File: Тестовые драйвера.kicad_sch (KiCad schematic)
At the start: 172 parts, among them J1 Conn_01x01, J2 Conn_01x01, J3 Conn_01x01, J4 Conn_01x01, J5 Conn_01x01, J6 Conn_02x10_Odd_Even, J7 Conn_02x10_Odd_Even, Q1 C2M0280120D, Q2 C2M0280120D, Q3 C2M0280120D, Q4 C2M0280120D, Q5 C2M0280120D, Q6 C2M0280120D, U1 74AHC1G08, U2 74AHC1G08, U3 74AHC1G08

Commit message: Расположил на плате
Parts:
- C4: footprint Capacitor_SMD:C_0603_1608Metric_Pad1.08x0.95mm_HandSolder -> Capacitor_SMD:C_0805_2012Metric_Pad1.18x1.45mm_HandSolder
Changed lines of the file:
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@@
       (effects (font (size 1.27 1.27)) (justify left))
     )
-    (property "Footprint" "Capacitor_SMD:C_0603_1608Metric_Pad1.08x0.95mm_HandSolder" (at 50.8 106.045 0)
+    (property "Footprint" "Capacitor_SMD:C_0805_2012Metric_Pad1.18x1.45mm_HandSolder" (at 50.8 106.045 0)
       (effects (font (size 1.27 1.27)) hide)
     )
@@
       (effects (font (size 1.27 1.27)) (justify left))
     )
-    (property "Footprint" "Capacitor_SMD:C_0603_1608Metric_Pad1.08x0.95mm_HandSolder" (at 50.8 43.815 0)
+    (property "Footprint" "Capacitor_SMD:C_0805_2012Metric_Pad1.18x1.45mm_HandSolder" (at 50.8 43.815 0)
       (effects (font (size 1.27 1.27)) hide)
     )
@@
       (effects (font (size 1.27 1.27)) (justify left))
     )
-    (property "Footprint" "Capacitor_SMD:C_0603_1608Metric_Pad1.08x0.95mm_HandSolder" (at 50.8 207.645 0)
+    (property "Footprint" "Capacitor_SMD:C_0805_2012Metric_Pad1.18x1.45mm_HandSolder" (at 50.8 207.645 0)
       (effects (font (size 1.27 1.27)) hide)
     )
@@
       (effects (font (size 1.27 1.27)) (justify left))
     )
-    (property "Footprint" "Capacitor_SMD:C_0603_1608Metric_Pad1.08x0.95mm_HandSolder" (at 59.055 74.93 0)
+    (property "Footprint" "Capacitor_SMD:C_0805_2012Metric_Pad1.18x1.45mm_HandSolder" (at 59.055 74.93 0)
       (effects (font (size 1.27 1.27)) hide)
     )
@@
       (effects (font (size 1.27 1.27)) (justify left))
     )
-    (property "Footprint" "Capacitor_SMD:C_0603_1608Metric_Pad1.08x0.95mm_HandSolder" (at 59.055 207.645 0)
+    (property "Footprint" "Capacitor_SMD:C_0805_2012Metric_Pad1.18x1.45mm_HandSolder" (at 59.055 207.645 0)
       (effects (font (size 1.27 1.27)) hide)
     )
@@
       (effects (font (size 1.27 1.27)) (justify left))
     )
-    (property "Footprint" "Capacitor_SMD:C_0603_1608Metric_Pad1.08x0.95mm_HandSolder" (at 59.055 106.045 0)
+    (property "Footprint" "Capacitor_SMD:C_0805_2012Metric_Pad1.18x1.45mm_HandSolder" (at 59.055 106.045 0)
       (effects (font (size 1.27 1.27)) hide)
     )
@@
       (effects (font (size 1.27 1.27)) (justify left))
     )
-    (property "Footprint" "Capacitor_SMD:C_0603_1608Metric_Pad1.08x0.95mm_HandSolder" (at 59.055 146.685 0)
+    (property "Footprint" "Capacitor_SMD:C_0805_2012Metric_Pad1.18x1.45mm_HandSolder" (at 59.055 146.685 0)
       (effects (font (size 1.27 1.27)) hide)
     )
@@
       (effects (font (size 1.27 1.27)) (justify left))
     )
-    (property "Footprint" "Capacitor_SMD:C_0603_1608Metric_Pad1.08x0.95mm_HandSolder" (at 50.8 146.685 0)
+    (property "Footprint" "Capacitor_SMD:C_0805_2012Metric_Pad1.18x1.45mm_HandSolder" (at 50.8 146.685 0)
       (effects (font (size 1.27 1.27)) hide)
     )
@@
       (effects (font (size 1.27 1.27)) (justify left))
     )
-    (property "Footprint" "Capacitor_SMD:C_0603_1608Metric_Pad1.08x0.95mm_HandSolder" (at 59.055 43.815 0)
+    (property "Footprint" "Capacitor_SMD:C_0805_2012Metric_Pad1.18x1.45mm_HandSolder" (at 59.055 43.815 0)
       (effects (font (size 1.27 1.27)) hide)
     )
@@
       (effects (font (size 1.27 1.27)) (justify left))
     )
-    (property "Footprint" "Capacitor_SMD:C_0603_1608Metric_Pad1.08x0.95mm_HandSolder" (at 50.8 177.165 0)
+    (property "Footprint" "Capacitor_SMD:C_0805_2012Metric_Pad1.18x1.45mm_HandSolder" (at 50.8 177.165 0)
       (effects (font (size 1.27 1.27)) hide)
     )
@@
       (effects (font (size 1.27 1.27)) (justify left))
     )
-    (property "Footprint" "Capacitor_SMD:C_0603_1608Metric_Pad1.08x0.95mm_HandSolder" (at 59.055 177.165 0)
+    (property "Footprint" "Capacitor_SMD:C_0805_2012Metric_Pad1.18x1.45mm_HandSolder" (at 59.055 177.165 0)
       (effects (font (size 1.27 1.27)) hide)
     )
@@
       (effects (font (size 1.27 1.27)) (justify left))
     )
-    (property "Footprint" "Capacitor_SMD:C_0603_1608Metric_Pad1.08x0.95mm_HandSolder" (at 50.8 74.93 0)
+    (property "Footprint" "Capacitor_SMD:C_0805_2012Metric_Pad1.18x1.45mm_HandSolder" (at 50.8 74.93 0)
       (effects (font (size 1.27 1.27)) hide)
     )

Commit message: Закончил схему и разводку платы
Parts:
- removed C9 (x3): 56p, Capacitor_SMD:C_0603_1608Metric_Pad1.08x0.95mm_HandSolder, symbol Device:C_Small
- removed C9 (x2): 1u, Capacitor_SMD:C_0603_1608Metric_Pad1.08x0.95mm_HandSolder, symbol Device:C_Small
- removed J7: Conn_02x10_Odd_Even, Connector_PinHeader_2.54mm:PinHeader_2x10_P2.54mm_Vertical, symbol Connector_Generic:Conn_02x10_Odd_Even
- removed R5 (x3): 120, Resistor_SMD:R_0805_2012Metric_Pad1.20x1.40mm_HandSolder, symbol Device:R_Small
- removed U1, U2, U3: 74AHC1G08, Package_SO:TSOP-5_1.65x3.05mm_P0.95mm, symbol 74xGxx:74AHC1G08
- added D15, D16: MBR0520, Diode_My:D_SOD_123_Hand, symbol Device:D_Small
- added R5 (x2): 120, Resistor_SMD:R_0805_2012Metric_Pad1.20x1.40mm_HandSolder, symbol Device:R_Small
- added R5: 1k, Resistor_SMD:R_0805_2012Metric_Pad1.20x1.40mm_HandSolder, symbol Device:R_Small
- added R5: 2k, Resistor_SMD:R_0805_2012Metric_Pad1.20x1.40mm_HandSolder, symbol Device:R_Small
- added R56, R57: 0.5m, Shunt_My:LR2725, symbol Device:R
- added TP26: TestPoint, TestPoint:TestPoint_Loop_D2.50mm_Drill1.0mm_LowProfile, symbol Connector:TestPoint
- added U3: HEF4082BT, Package_SO:SO-14_3.9x8.65mm_P1.27mm, symbol HEF4082BT_652:HEF4082BT,652
- C60, C61, C62: footprint Capacitor_SMD:C_0603_1608Metric_Pad1.08x0.95mm_HandSolder -> Capacitor_SMD:C_1210_3225Metric_Pad1.33x2.70mm_HandSolder
- C9: footprint Capacitor_SMD:C_0603_1608Metric_Pad1.08x0.95mm_HandSolder -> Capacitor_SMD:C_0805_2012Metric_Pad1.18x1.45mm_HandSolder
- J1, J2, J3: footprint Connector_My:Power_Wire -> Connector_Power_My:Cuprum_M4
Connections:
- net CommonERR is gone; now on net GND: J6.17 (Pin_17)
- net +3.3V: now also J6.3 (Pin_3), J6.5 (Pin_5), J6.7 (Pin_7), J6.9 (Pin_9), U3.11 (2C), U3.12 (2D), U3.14 (VDD), U3.4 (1C), U3.5 (1D)
- net GND: now also C9.1, J6.11 (Pin_11), J6.13 (Pin_13), J6.15 (Pin_15), J6.19 (Pin_19), R5.1, R5.1, U3.7 (VSS); no longer C9.2, J4.1 (Pin_1), J6.2 (Pin_2)
- net GND1: now also J4.1 (Pin_1)
- net GND2H: now also R57.2; no longer D3.1 (K), J2.1 (Pin_1), Q4.2 (D), Q5.2 (D), Q6.2 (D), TP17.1, TP20.1, TP23.1
- net GNDPWR: now also TP26.1
- net HighERR: now also J6.10 (Pin_10), D15.2 (A); no longer J6.13 (Pin_13)
- net IN+H: now also J6.4 (Pin_4); no longer J6.5 (Pin_5)
- net IN+L: now also J6.16 (Pin_16); no longer J6.6 (Pin_6)
- net IN-H: now also J6.6 (Pin_6); no longer J6.7 (Pin_7)
- net IN-L: now also J6.18 (Pin_18); no longer J6.8 (Pin_8)
- net LowERR: now also C9.2, J6.8 (Pin_8), D16.2 (A); no longer C9.1, J6.15 (Pin_15)
- net RDYH: no longer J6.9 (Pin_9)
- net RDYL: no longer J6.10 (Pin_10)
- net ~{FLTH}: no longer J6.11 (Pin_11)
- net ~{FLTL}: no longer J6.12 (Pin_12)
- net ~{RSTH}: now also J6.2 (Pin_2); no longer J6.3 (Pin_3)
- net ~{RSTL}: now also J6.20 (Pin_20); no longer J6.4 (Pin_4)
- net HighERR_ADC: now reaches J6.14 (Pin_14)
- net HighERR_ADC: now also R5.2, R5.2
- net at R5.2: now also U3.13 (2Y)
- net at C9.1, R5.1: now also U3.10 (2B)
- net at C9.1, R5.1: now also U3.9 (2A)
- net at C9.1, R5.1: now also U3.3 (1B)
- net at C9.1, R5.1: now also U3.2 (1A)
- net at R5.2: now also U3.1 (1Y)
- new net: D15.1 (K), R5.1
- new net: D16.1 (K), R5.1
- new net Drain_Low: D3.1 (K), Q4.2 (D), Q5.2 (D), Q6.2 (D), R56.2, TP17.1, TP20.1, TP23.1
- new net LowERR_ADC: J6.12 (Pin_12), R5.2, R5.2
- new net OUT: J2.1 (Pin_1), R56.1, R57.1
- no-connect marks 0 -> 2
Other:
- note added: "ERROR"
- note removed: "Общая ошибка"
- note removed: "Опции ERROR"
- note removed: "Ошибка верхнего драйвера"
- note removed: "Ошибка нижнего драйвера"
- moved on the sheet: C9, J6, R5, TP7

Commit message: Пытаюсь сделать как у вольфспида
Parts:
- removed C60, C61: 4.7u, Capacitor_SMD:C_1210_3225Metric_Pad1.33x2.70mm_HandSolder, symbol Device:C_Small
- removed C61: 10u, Capacitor_SMD:C_1210_3225Metric_Pad1.33x2.70mm_HandSolder, symbol Device:C_Small
- removed C62 (x3): CY-270p, Capacitor_SMD:C_1210_3225Metric_Pad1.33x2.70mm_HandSolder, symbol Device:C_Small
- removed C8 (x2), C9 (x2): 0.1n, Capacitor_SMD:C_0805_2012Metric_Pad1.18x1.45mm_HandSolder, symbol Device:C_Small
- removed C9 (x6): 56p, Capacitor_SMD:C_0805_2012Metric_Pad1.18x1.45mm_HandSolder, symbol Device:C_Small
- removed C9: 1u, Capacitor_SMD:C_0805_2012Metric_Pad1.18x1.45mm_HandSolder, symbol Device:C_Small
- removed D12, D5: D_Zener_Small, Diode_SMD:D_SMA-SMB_Universal_Handsoldering, symbol Device:D_Zener_Small
- removed D13, D6, D7: LED_Small, LED_SMD:LED_0805_2012Metric_Pad1.15x1.40mm_HandSolder, symbol Device:LED_Small
- removed D15, D16: MBR0520, Diode_My:D_SOD_123_Hand, symbol Device:D_Small
- removed D2 (x2): D_Small, Diode_SMD:D_SMA_Handsoldering, symbol Device:D_Small
- removed J6: Conn_02x10_Odd_Even, Connector_PinSocket_2.54mm:PinSocket_2x10_P2.54mm_Vertical, symbol Connector_Generic:Conn_02x10_Odd_Even
- removed L2: 6.8u, Inductor_SMD:L_1812_4532Metric_Pad1.30x3.40mm_HandSolder, symbol Device:L_Small
- removed PS1, PS2: A1215S-1WR3, Converter_DCDC:Converter_DCDC_XP_POWER-IAxxxxS_THT, symbol Converter_DCDC:IA1215S
- removed PS3: B1203S-1WR3, Converter_DCDC:Converter_DCDC_RECOM_R-78S-0.1_THT, symbol Converter_DCDC:IA1203S
- removed R4 (x2): Rdesat, Resistor_SMD:R_0805_2012Metric_Pad1.20x1.40mm_HandSolder, symbol Device:R_Small
- removed R5 (x8): 120, Resistor_SMD:R_0805_2012Metric_Pad1.20x1.40mm_HandSolder, symbol Device:R_Small
- removed R5 (x4): 330, Resistor_SMD:R_0805_2012Metric_Pad1.20x1.40mm_HandSolder, symbol Device:R_Small
- removed R5: 1k, Resistor_SMD:R_0805_2012Metric_Pad1.20x1.40mm_HandSolder, symbol Device:R_Small
- removed R5: 2k, Resistor_SMD:R_0805_2012Metric_Pad1.20x1.40mm_HandSolder, symbol Device:R_Small
- removed R5 (x2), R6 (x2): 4.7k, Resistor_SMD:R_0805_2012Metric_Pad1.20x1.40mm_HandSolder, symbol Device:R_Small
- removed R56, R57: 0.5m, Shunt_My:LR2725, symbol Device:R
- removed TP15, TP16, TP5, TP6: TestPoint, TestPoint:TestPoint_Loop_D2.50mm_Drill1.0mm_LowProfile, symbol Connector:TestPoint
- removed U3: HEF4082BT, Package_SO:SO-14_3.9x8.65mm_P1.27mm, symbol HEF4082BT_652:HEF4082BT,652
- added C11, C23: 100p, Capacitor_SMD:C_1206_3216Metric_Pad1.33x1.80mm_HandSolder, symbol Device:C_Small
- added C28, C29: 10u, Capacitor_SMD:C_1210_3225Metric_Pad1.33x2.70mm_HandSolder, symbol Device:C_Small
- added C39, C40: 2.2u, Capacitor_SMD:C_0805_2012Metric_Pad1.18x1.45mm_HandSolder, symbol Device:C_Small
- added C45, C46: 56p, Capacitor_SMD:C_0805_2012Metric_Pad1.18x1.45mm_HandSolder, symbol Device:C_Small
- added D10, D11: D_Small, Diode_SMD:D_SMB_Handsoldering, symbol Device:D_Small
- added D12: ~, Package_SO:SOIC-8_3.9x4.9mm_P1.27mm, symbol Interface_My:ADM3485E
- added D13: ~, Package_TO_SOT_SMD:SOT-23-5, symbol Logic_My:SN74AHC1G08DBVR
- added D15: ~, LED_SMD:LED_0805_2012Metric_Pad1.15x1.40mm_HandSolder, symbol Device:LED_Small
- added D16, D17: ~, QAxCx, symbol Mornsun:QAxCx
- added D4, D5: ~, Diode_SMD:D_SOD-123, symbol Device:D_Schottky_Small
- added D6: ~, Mornsun:K78xxM-1000R3, symbol Mornsun:K78xxM-1000R3 ÕýÊä³ö
- added J6: ~, Connector_Molex:Molex_Micro-Fit_3.0_43045-1212_2x06_P3.00mm_Vertical, symbol Connector_Generic:Conn_02x06_Top_Bottom
- added Q7: ~, Package_TO_SOT_SMD:SOT-23, symbol Transistor_FET:2N7002
- added R40: 120, Resistor_SMD:R_0805_2012Metric_Pad1.20x1.40mm_HandSolder, symbol Device:R_Small
- added R41, R48, R50: 1k, Resistor_SMD:R_0805_2012Metric_Pad1.20x1.40mm_HandSolder, symbol Device:R_Small
- added R42: 4.7k, Resistor_SMD:R_0805_2012Metric_Pad1.20x1.40mm_HandSolder, symbol Device:R_Small
- added R49: 10k, Resistor_SMD:R_0805_2012Metric_Pad1.20x1.40mm_HandSolder, symbol Device:R_Small
- added R51: 560, Resistor_SMD:R_0805_2012Metric_Pad1.20x1.40mm_HandSolder, symbol Device:R_Small
- C1: renamed from C57; value 0.47u -> 10u; footprint Capacitor_SMD:C_1210_3225Metric_Pad1.33x2.70mm_HandSolder -> Capacitor_SMD:C_1206_3216Metric_Pad1.33x1.80mm_HandSolder
- C12, C32: renamed from C3; value Cblk -> 100p
- C15: renamed from C63; value 0.47u -> 10u; footprint Capacitor_SMD:C_1210_3225Metric_Pad1.33x2.70mm_HandSolder -> Capacitor_SMD:C_1206_3216Metric_Pad1.33x1.80mm_HandSolder
- C16, C35: renamed from C4; footprint Capacitor_SMD:C_0805_2012Metric_Pad1.18x1.45mm_HandSolder -> Capacitor_SMD:C_1206_3216Metric_Pad1.33x1.80mm_HandSolder
- C17, C36: renamed from C5; footprint Capacitor_SMD:C_0805_2012Metric_Pad1.18x1.45mm_HandSolder -> Capacitor_SMD:C_1206_3216Metric_Pad1.33x1.80mm_HandSolder
- C18: renamed from C60; footprint Capacitor_SMD:C_1210_3225Metric_Pad1.33x2.70mm_HandSolder -> Capacitor_SMD:C_1206_3216Metric_Pad1.33x1.80mm_HandSolder
- C19: renamed from C61; footprint Capacitor_SMD:C_1210_3225Metric_Pad1.33x2.70mm_HandSolder -> Capacitor_SMD:C_1206_3216Metric_Pad1.33x1.80mm_HandSolder
- C2: footprint Capacitor_SMD:C_0805_2012Metric_Pad1.18x1.45mm_HandSolder -> Capacitor_SMD:C_1206_3216Metric_Pad1.33x1.80mm_HandSolder
- C20: renamed from C64; value 0.47u -> 10u; footprint Capacitor_SMD:C_1210_3225Metric_Pad1.33x2.70mm_HandSolder -> Capacitor_SMD:C_1206_3216Metric_Pad1.33x1.80mm_HandSolder
- C21, C26, C37, C41, C43, C9: renamed from C4; value 100n -> 10n
- C24: renamed from C2; footprint Capacitor_SMD:C_0805_2012Metric_Pad1.18x1.45mm_HandSolder -> Capacitor_SMD:C_1206_3216Metric_Pad1.33x1.80mm_HandSolder
- C25, C3: renamed from C1; footprint Capacitor_SMD:C_0805_2012Metric_Pad1.18x1.45mm_HandSolder -> Capacitor_SMD:C_1206_3216Metric_Pad1.33x1.80mm_HandSolder
- C4: renamed from C56; footprint Capacitor_SMD:C_1210_3225Metric_Pad1.33x2.70mm_HandSolder -> Capacitor_SMD:C_1206_3216Metric_Pad1.33x1.80mm_HandSolder
- C5: renamed from C55; footprint Capacitor_SMD:C_1210_3225Metric_Pad1.33x2.70mm_HandSolder -> Capacitor_SMD:C_1206_3216Metric_Pad1.33x1.80mm_HandSolder
- C6: renamed from C58; value 0.47u -> 10u; footprint Capacitor_SMD:C_1210_3225Metric_Pad1.33x2.70mm_HandSolder -> Capacitor_SMD:C_1206_3216Metric_Pad1.33x1.80mm_HandSolder
- D14: value LED_Small -> ~; Description P/N (none) -> Red LED; Product Name (none) -> FYLS-0805URC; Purpose (none) -> FLT
- D2: renamed from D3; footprint Diode_SMD:D_SMA_Handsoldering -> Diode_SMD:D_SMB_Handsoldering
- D3: renamed from D4; footprint Diode_SMD:D_SMA-SMB_Universal_Handsoldering -> Diode_SMD:D_SOD-323_HandSoldering
- D9: renamed from D11; footprint Diode_SMD:D_SMA-SMB_Universal_Handsoldering -> Diode_SMD:D_SOD-323_HandSoldering
- L1, L2: value 6.8u -> 22u
- Q1, Q2, Q3, Q4, Q5, Q6: footprint Package_TO_SOT_THT:TO-220-3_Horizontal_TabUp -> Package_TO_SOT_THT:TO-247-3_Horizontal_TabUp
- renumbered C4 to C10, C4 to C22, C4 to C27, C6 to C30, C7 to C31, C4 to C38, C4 to C42, C4 to C44, C6 to C7, C7 to C8, D1 to D7, D3 to D8, R1 to R11, R1 to R12, R1 to R13, R4 to R14, R1 to R15, R1 to R16, R1 to R17, R1 to R18, R4 to R19, R1 to R2, R1 to R20, R3 to R21, R1 to R26, R6 to R27, R6 to R28, R6 to R29, R1 to R3, R6 to R30, R1 to R31, R1 to R32, R4 to R33, R1 to R34, R1 to R35, R1 to R36, R1 to R37, R4 to R38, R1 to R39, R1 to R43, R1 to R44, R1 to R45, R4 to R46, R1 to R47, R1 to R5, R3 to R6, TP26 to TP17, TP17 to TP18, TP18 to TP19, TP19 to TP20, TP20 to TP21, TP21 to TP22, TP22 to TP23, TP23 to TP24, TP24 to TP25, TP25 to TP26, TP8 to TP7, TP7 to TP8
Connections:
- net RDYL is gone; now on net RDY: D7.12 (RDY)
- net ~{FLTH} is gone; now on net ~{FLT}: D1.13 (~{FLT})
- net ~{FLTL} is gone; now on net ~{FLT}: D7.13 (~{FLT})
- net +12V: no longer C18.1, C4.1, L1.1, L2.1
- net +15VH: now also D16.7 (+Vo)
- net +15VL: now also D17.7 (+Vo)
- net -15VL: now also D17.5 (-Vo)
- net ClampH: now also R1.2, R11.2, R15.1, R16.2, R20.1, R5.1
- net ClampL: now also R26.2, R34.1, R35.2, R39.1, R43.2, R47.1
- net Drain_Low: now also D11.1 (K); no longer D8.1 (K)
- net GND: now also C28.2, C29.2, C39.2, C40.2, C45.2, C46.2, D12.5 (GND), D13.3 (GND), D15.1 (K), D6.2 (GND), J6.8 (Pin_8), Q7.2 (S)
- net GND1: now also C11.2, C23.2, D16.2 (GND), D17.2 (GND)
- net GND2H: now also D16.6 (0V), D4.2 (A)
- net GNDPWR: now also D17.6 (0V), D5.2 (A)
- net IN+H: no longer D1.10 (IN+)
- net IN+L: no longer D7.10 (IN+)
- net IN-H: no longer D1.11 (IN-)
- net IN-L: no longer D7.11 (IN-)
- net OutH1: now also R12.1, R17.1, R2.1
- net OutH2: now also R31.1, R36.1, R44.1
- net OutL1: now also R13.2, R18.2, R3.2
- net OutL2: now also R32.2, R37.2, R45.2
- net VDC: now also D10.1 (K); no longer D2.1 (K)
- net ~{RSTH}: no longer D1.14 (~{RST})
- net ~{RSTL}: no longer D7.14 (~{RST})
- net at C19.1, L2.2: now also C23.1, D17.1 (Vin)
- net at C12.2, D1.2 (DESAT), R6.2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: now also D4.1 (K)
- net at D8.2 (A): now also D9.2 (A)
- net at C5.1, L1.2: now also C11.1, D16.1 (Vin)
- net at D3.1 (K): now also R6.1
- net ~{FLT}: now reaches D14.1 (K)
- net ~{FLT}: now also C46.1, D13.2 (A), R49.1
- net at C32.2, D7.2 (DESAT), R21.2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: now also D5.1 (K)
- net at R21.1: now also D9.1 (K)
- net at D2.2 (A): now also D3.2 (A)
- net +3.3V renamed +5V
- net +5V: now also C29.1, C39.1, C40.1, D12.2 (RE), D12.3 (DE), D12.8 (VCC), D13.5 (Vcc), D6.3 (+Vo), R41.2, R48.2, R49.2, R50.2; no longer D14.2 (A)
- net -15VH renamed -4VH
- net -4VH: now also D16.5 (-Vo)
- net RDYH renamed RDY
- net RDY: now also C45.1, D13.1 (B), R48.1, R51.2
- new net: D14.2 (A), R50.1
- new net: D10.2 (A), D2.1 (K)
- new net: D15.2 (A), R51.1
- new net: D11.2 (A), D8.1 (K)
- new net: D12.4 (DI), D13.4 (Y)
- new net: Q7.1 (G), R42.2
- new net +15V: C18.1, C28.1, C4.1, D6.1 (Vin), J6.2 (Pin_2), L1.1, L2.1
- new net Fault_N: D12.7 (B), J6.10 (Pin_10), R40.1
- new net Fault_P: D12.6 (A), J6.4 (Pin_4), R40.2
- new net PWM_N: D1.11 (IN-), D7.10 (IN+), J6.9 (Pin_9)
- new net PWM_P: D1.10 (IN+), D7.11 (IN-), J6.3 (Pin_3)
- new net RST: D1.14 (~{RST}), D7.14 (~{RST}), Q7.3 (D), R41.1
- new net Reset: J6.6 (Pin_6), R42.1
- no-connect marks 2 -> 6
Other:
- note added: "Питание 5В"
- note added: "Сброс ошибки драйвера"
- note removed: "Питание 3.3В опционально"
- moved on the sheet: C10, C12, C18, C19, C21, C22, C24, C25, C26, C27, C30, C31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

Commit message: VER1.0: пробую уложиться в ширину транзисторов
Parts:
- removed C10, C22, C27, C38, C42, C44: Cf, Capacitor_SMD:C_0805_2012Metric_Pad1.18x1.45mm_HandSolder, symbol Device:C_Small
- removed TP1, TP10, TP11, TP12, TP13, TP14, TP17, TP18, TP19, TP2, TP20, TP21, TP22, TP23, TP24, TP25, TP26, TP3, TP4, TP7, TP8, TP9: TestPoint, TestPoint:TestPoint_Loop_D2.50mm_Drill1.0mm_LowProfile, symbol Connector:TestPoint
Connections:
- net GND2H: now also R14.1, R19.1, R4.1
- net GNDPWR: now also R33.1, R38.1, R46.1
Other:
- moved on the sheet: R14, R19, R33, R38, R4, R46

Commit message: Пытаюсь уложиться в контур транзисторов
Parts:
- removed C1, C15, C20, C6: 10u, Capacitor_SMD:C_1206_3216Metric_Pad1.33x1.80mm_HandSolder, symbol Device:C_Small
- removed J4, J5: Conn_01x01, Connector_My:Power_Wire, symbol Connector_Generic:Conn_01x01
- J1, J2, J3: footprint Connector_Power_My:Cuprum_M4 -> Bush_my:Bush_SMD_M3
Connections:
- net OUT is gone; now on net GND2H: J2.1 (Pin_1)
- net Drain_Low: no longer Q4.2 (D), Q5.2 (D), Q6.2 (D)
- net GND2H: now also Q4.2 (D), Q5.2 (D), Q6.2 (D)
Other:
- moved on the sheet: J1, J2, J3

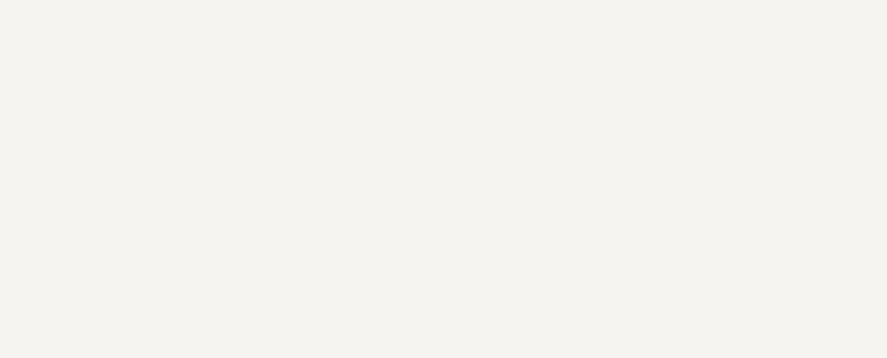
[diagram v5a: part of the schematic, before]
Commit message: VER1.0: разделил плату драйвера и силовую
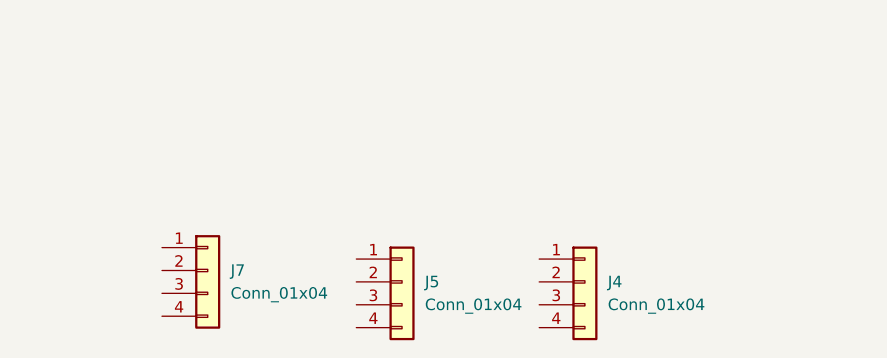
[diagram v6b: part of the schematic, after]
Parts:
- added J4, J5, J7: Conn_01x04, Connector_PinSocket_2.54mm:PinSocket_1x04_P2.54mm_Vertical, symbol Connector_Generic:Conn_01x04
- R14, R19, R33, R38, R4, R46: value Rdesat -> 10k
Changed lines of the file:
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@@
 	)
 	(symbol
+		(lib_id "Connector_Generic:Conn_01x04")
+		(at 215.9 256.54 0)
+		(unit 1)
+		(exclude_from_sim no)
+		(in_bom yes)
+		(on_board yes)
+		(dnp no)
+		(fields_autoplaced yes)
+		(property "Reference" "J5"
+			(at 218.44 256.54 0)
+			(effects
+				(font
+					(size 1.27 1.27)
+				)
+				(justify left)
+			)
+		)
+		(property "Value" "Conn_01x04"
+			(at 218.44 259.08 0)
+			(effects
+				(font
+					(size 1.27 1.27)
+				)
+				(justify left)
+			)
+		)
+		(property "Footprint" "Connector_PinSocket_2.54mm:PinSocket_1x04_P2.54mm_Vertical"
+			(at 215.9 256.54 0)
+			(effects
+				(font
+					(size 1.27 1.27)
+				)
+				(hide yes)
+			)
+		)
+		(property "Datasheet" "~"
+			(at 215.9 256.54 0)
+			(effects
+				(font
+					(size 1.27 1.27)
+				)
+				(hide yes)
+			)
+		)
+		(property "Description" "Generic connector, single row, 01x04, script generated (kicad-library-utils/schlib/autogen/connector/)"
+			(at 215.9 256.54 0)
+			(effects
+				(font
+					(size 1.27 1.27)
+				)
+				(hide yes)
+			)
+		)
+		(pin "3"
+		)
+		(pin "4"
+		)
+		(pin "2"
+		)
+		(pin "1"
+		)
+		(instances
+			(project "Тестовые драйвера"
+				(path "/d1e1d0ee-338f-4b8c-beae-d34a6382fd09"
+					(reference "J5")
+					(unit 1)
+				)
+			)
+		)
+	)
+	(symbol
 		(lib_id "Device:C_Small")
 		(at 175.26 64.77 0)
@@
 			)
 		)
-		(property "Value" "Rdesat"
+		(property "Value" "10k"
 			(at 62.23 40.64 90)
 			(effects
@@
 	)
 	(symbol
+		(lib_id "Connector_Generic:Conn_01x04")
+		(at 194.31 255.27 0)
+		(unit 1)
+		(exclude_from_sim no)
+		(in_bom yes)
+		(on_board yes)
+		(dnp no)
+		(fields_autoplaced yes)
+		(property "Reference" "J7"
+			(at 196.85 255.27 0)
+			(effects
+				(font
+					(size 1.27 1.27)
+				)
+				(justify left)
+			)
+		)
+		(property "Value" "Conn_01x04"
+			(at 196.85 257.81 0)
+			(effects
+				(font
+					(size 1.27 1.27)
+				)
+				(justify left)
+			)
+		)
+		(property "Footprint" "Connector_PinSocket_2.54mm:PinSocket_1x04_P2.54mm_Vertical"
+			(at 194.31 255.27 0)
+			(effects
+				(font
+					(size 1.27 1.27)
+				)
+				(hide yes)
+			)
+		)
+		(property "Datasheet" "~"
+			(at 194.31 255.27 0)
+			(effects
+				(font
+					(size 1.27 1.27)
+				)
+				(hide yes)
+			)
+		)
+		(property "Description" "Generic connector, single row, 01x04, script generated (kicad-library-utils/schlib/autogen/connector/)"
+			(at 194.31 255.27 0)
+			(effects
+				(font
+					(size 1.27 1.27)
+				)
+				(hide yes)
+			)
+		)
+		(pin "3"
+		)
+		(pin "4"
+		)
+		(pin "2"
+		)
+		(pin "1"
+		)
+		(instances
+			(project "Тестовые драйвера"
+				(path "/d1e1d0ee-338f-4b8c-beae-d34a6382fd09"
+					(reference "J7")
+					(unit 1)
+				)
+			)
+		)
+	)
+	(symbol
 		(lib_name "-15VH_1")
 		(lib_id "power_my:-15VH")
@@
 			)
 		)
-		(property "Value" "Rdesat"
+		(property "Value" "10k"
 			(at 62.23 102.87 90)
 			(effects
@@
 			)
 		)
-		(property "Value" "Rdesat"
+		(property "Value" "10k"
 			(at 62.23 204.47 90)
 			(effects
@@
 			)
 		)
-		(property "Value" "Rdesat"
+		(property "Value" "10k"
 			(at 62.23 143.51 90)
 			(effects
@@
 			)
 		)
-		(property "Value" "Rdesat"
+		(property "Value" "10k"
 			(at 62.23 71.12 90)
 			(effects
@@
 	)
 	(symbol
+		(lib_id "Connector_Generic:Conn_01x04")
+		(at 236.22 256.54 0)
+		(unit 1)
+		(exclude_from_sim no)
+		(in_bom yes)
+		(on_board yes)
+		(dnp no)
+		(fields_autoplaced yes)
+		(property "Reference" "J4"
+			(at 238.76 256.54 0)
+			(effects
+				(font
+					(size 1.27 1.27)
+				)
+				(justify left)
+			)
+		)
+		(property "Value" "Conn_01x04"
+			(at 238.76 259.08 0)
+			(effects
+				(font
+					(size 1.27 1.27)
+				)
+				(justify left)
+			)
+		)
+		(property "Footprint" "Connector_PinSocket_2.54mm:PinSocket_1x04_P2.54mm_Vertical"
+			(at 236.22 256.54 0)
+			(effects
+				(font
+					(size 1.27 1.27)
+				)
+				(hide yes)
+			)
+		)
+		(property "Datasheet" "~"
+			(at 236.22 256.54 0)
+			(effects
+				(font
+					(size 1.27 1.27)
+				)
+				(hide yes)
+			)
+		)
+		(property "Description" "Generic connector, single row, 01x04, script generated (kicad-library-utils/schlib/autogen/connector/)"
+			(at 236.22 256.54 0)
+			(effects
+				(font
+					(size 1.27 1.27)
+				)
+				(hide yes)
+			)
+		)
+		(pin "3"
+		)
+		(pin "4"
+		)
+		(pin "2"
+		)
+		(pin "1"
+		)
+		(instances
+			(project ""
+				(path "/d1e1d0ee-338f-4b8c-beae-d34a6382fd09"
+					(reference "J4")
+					(unit 1)
+				)
+			)
+		)
+	)
+	(symbol
 		(lib_id "power:GNDPWR")
 		(at 378.46 67.31 90)
@@
 			)
 		)
-		(property "Value" "Rdesat"
+		(property "Value" "10k"
 			(at 62.23 173.99 90)
 			(effects

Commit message: VER1.0: поработал над шинами
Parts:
- added J10, J11, J12, J13, J8, J9: Conn_01x01, Bush_my:Bush_5x3, symbol Connector_Generic:Conn_01x01
- added J14, J15, J16: Conn_01x03, Bush_my:247_border_my, symbol Connector_Generic:Conn_01x03
- J1, J2, J3: footprint Bush_my:Bush_SMD_M3 -> Bush_my:Bush_5x3
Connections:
- net Drain_Low is gone; now on net GNDPWR: D11.1 (K)
- net GND2H: now also J10.1 (Pin_1), J11.1 (Pin_1)
- net GNDPWR: now also J8.1 (Pin_1), J9.1 (Pin_1)
- net VDC: now also J12.1 (Pin_1), J13.1 (Pin_1)
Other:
- moved on the sheet: J1, J3
